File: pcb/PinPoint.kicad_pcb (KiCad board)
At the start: 2 copper layers, 35 x 32.5 mm, 2 parts, among them U1 E73-2G4M08S-52833

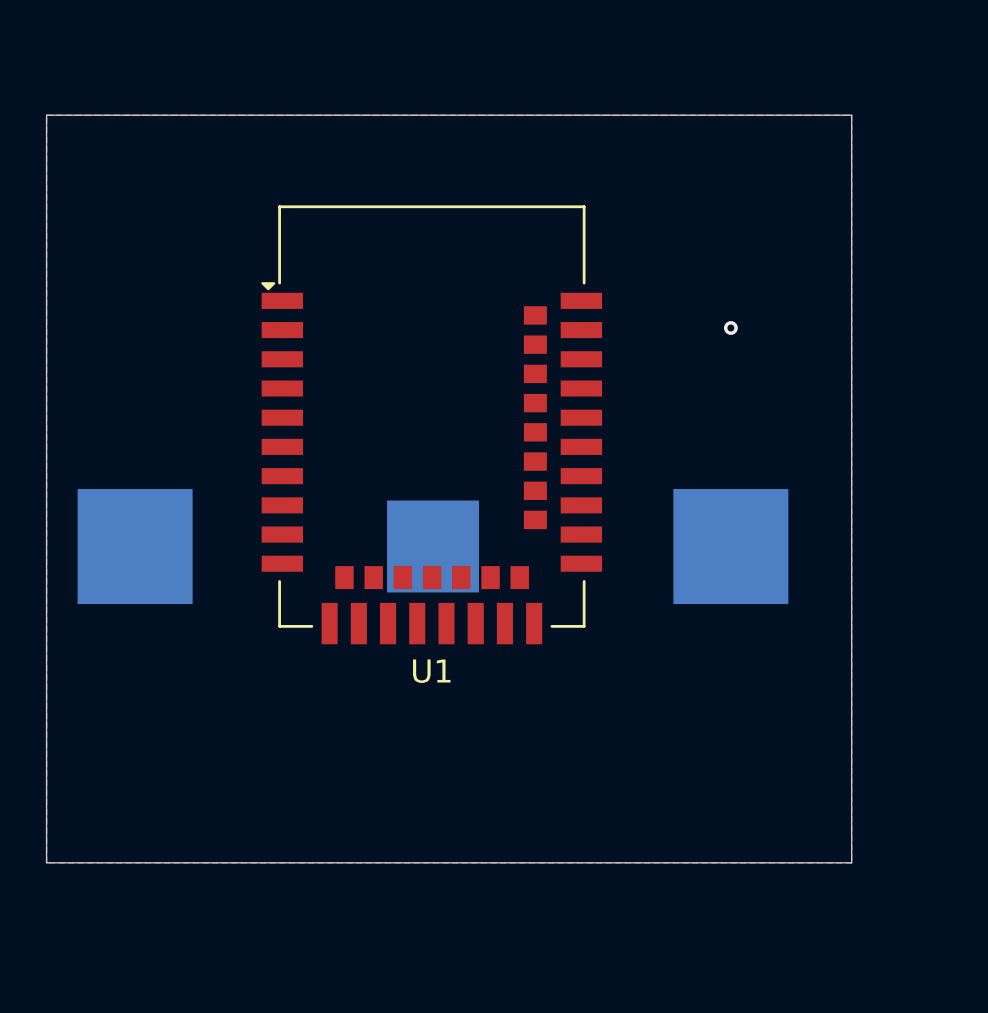
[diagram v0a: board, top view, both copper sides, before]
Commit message: Create board outline, change battery holder
Signed-off-by: Devnol <pgkoutsoumanis@gmail.com>
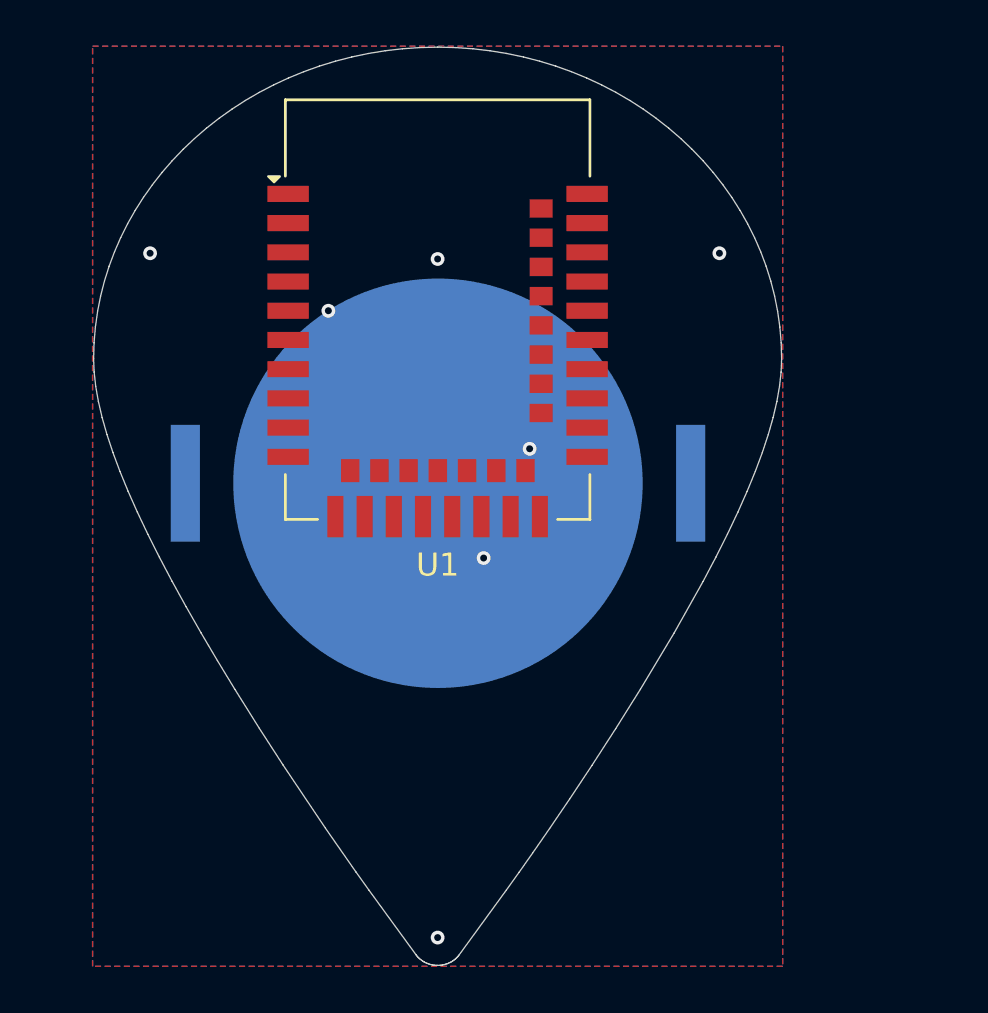
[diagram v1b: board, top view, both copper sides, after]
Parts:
- BT1: footprint Battery:BatteryHolder_Multicomp_BC-2001_1x2032 -> Battery:BatteryHolder_Keystone_3034_1x20mm
- moved U1 4.66 mm to (106.8, 41.2)
- moved BT1 2.76 mm to (106.8, 48.8)
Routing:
- net GND: vias 1 -> 7
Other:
- board size 35 x 32.5 mm -> 29.9 x 39.9 mm

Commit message: Add screw holes, debug port
Signed-off-by: Devnol <pgkoutsoumanis@gmail.com>
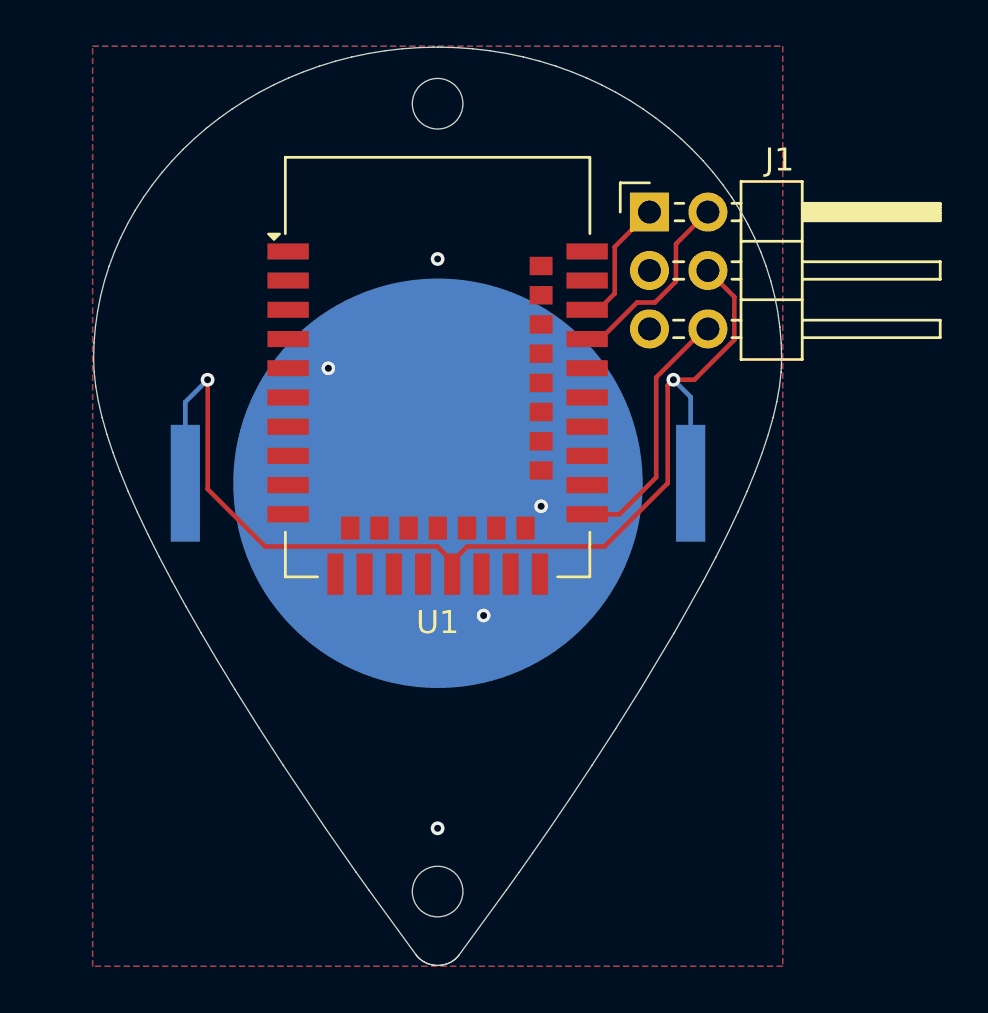
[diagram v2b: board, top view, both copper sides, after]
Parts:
- added J1: ~, Connector_PinHeader_2.54mm:PinHeader_2x03_P2.54mm_Horizontal, F.Cu at (116.0, 37.0)
- added REF**: MountingHole_2.2mm_M2_DIN965, MountingHole:MountingHole_2.2mm_M2_DIN965, F.Cu at (106.8, 32.2)
- added REF**: MountingHole_2.2mm_M2_DIN965, MountingHole:MountingHole_2.2mm_M2_DIN965, F.Cu at (106.8, 66.5)
- moved U1 2.50 mm to (106.8, 43.8)
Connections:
- net +BATT renamed VCC
- U1 pad 26: unconnected-(U1-P0.18/~{RESET}-Pad26) -> /~{RESET}
- U1 pad 37: unconnected-(U1-SWDIO-Pad37) -> /SWDIO
- U1 pad 39: unconnected-(U1-SWDCLK-Pad39) -> /SWDCLK
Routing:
- net VCC: track 0.00 -> 49.2 mm, vias 0 -> 2
- net /~{RESET}: track 0.00 -> 11.1 mm
- net /SWDIO: track 0.00 -> 8.49 mm
- net /SWDCLK: track 0.00 -> 5.66 mm
- net GND: vias 7 -> 5

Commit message: Add buzzer, include todo list for board features
Signed-off-by: Devnol <pgkoutsoumanis@gmail.com>
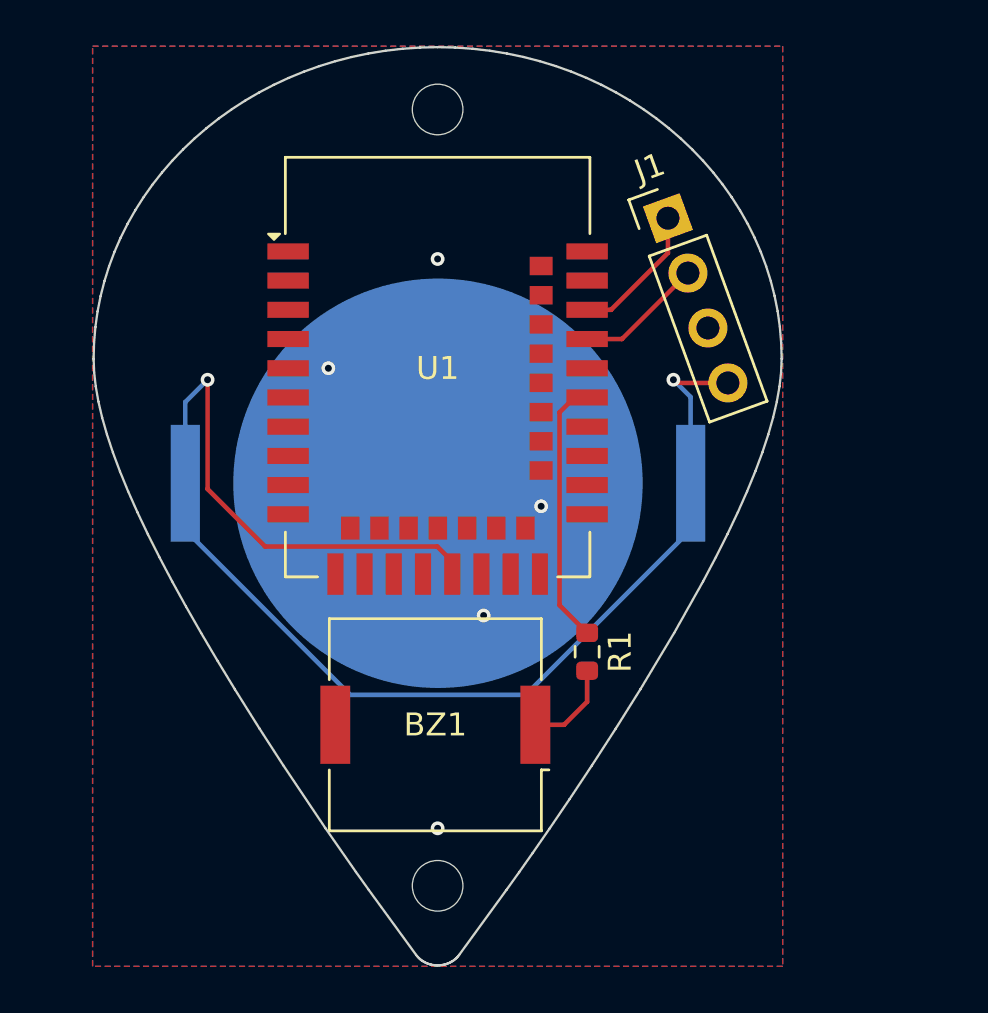
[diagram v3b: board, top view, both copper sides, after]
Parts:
- removed the REF** at (106.8, 32.2)
- removed the REF** at (106.8, 66.5)
- added BZ1: Buzzer, Buzzer_Beeper:Buzzer_Murata_PKMCS0909E, F.Cu at (106.7, 59.2)
- added R1: 100Ω, Resistor_SMD:R_0603_1608Metric, F.Cu at (113.2, 56.1)
- added REF**: MountingHole_2.2mm_M2_DIN965, MountingHole:MountingHole_2.2mm_M2_DIN965, F.Cu at (106.8, 66.2)
- added REF**: MountingHole_2.2mm_M2_DIN965, MountingHole:MountingHole_2.2mm_M2_DIN965, F.Cu at (106.8, 32.5)
- J1: footprint Connector_PinHeader_2.54mm:PinHeader_2x03_P2.54mm_Horizontal -> Connector_PinHeader_2.54mm:PinHeader_1x04_P2.54mm_Vertical
- moved J1 0.85 mm to (116.8, 37.2), turned to 20 degrees
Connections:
- U1 pad 26: /~{RESET} -> unconnected-(U1-P0.18/~{RESET}-Pad26)
- U1 pad 33: unconnected-(U1-P0.13-Pad33) -> Net-(U1-P0.13)
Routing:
- net VCC: track 49.2 -> 61.3 mm
- net Net-(U1-P0.13): track 0.00 -> 11.5 mm
- net /~{RESET}: track 11.1 -> 0.00 mm
- net Net-(BZ1-+): track 0.00 -> 4.01 mm
- net /SWDIO: track 8.49 -> 5.57 mm

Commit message: Jankily add microUSB port
Signed-off-by: Devnol <pgkoutsoumanis@gmail.com>
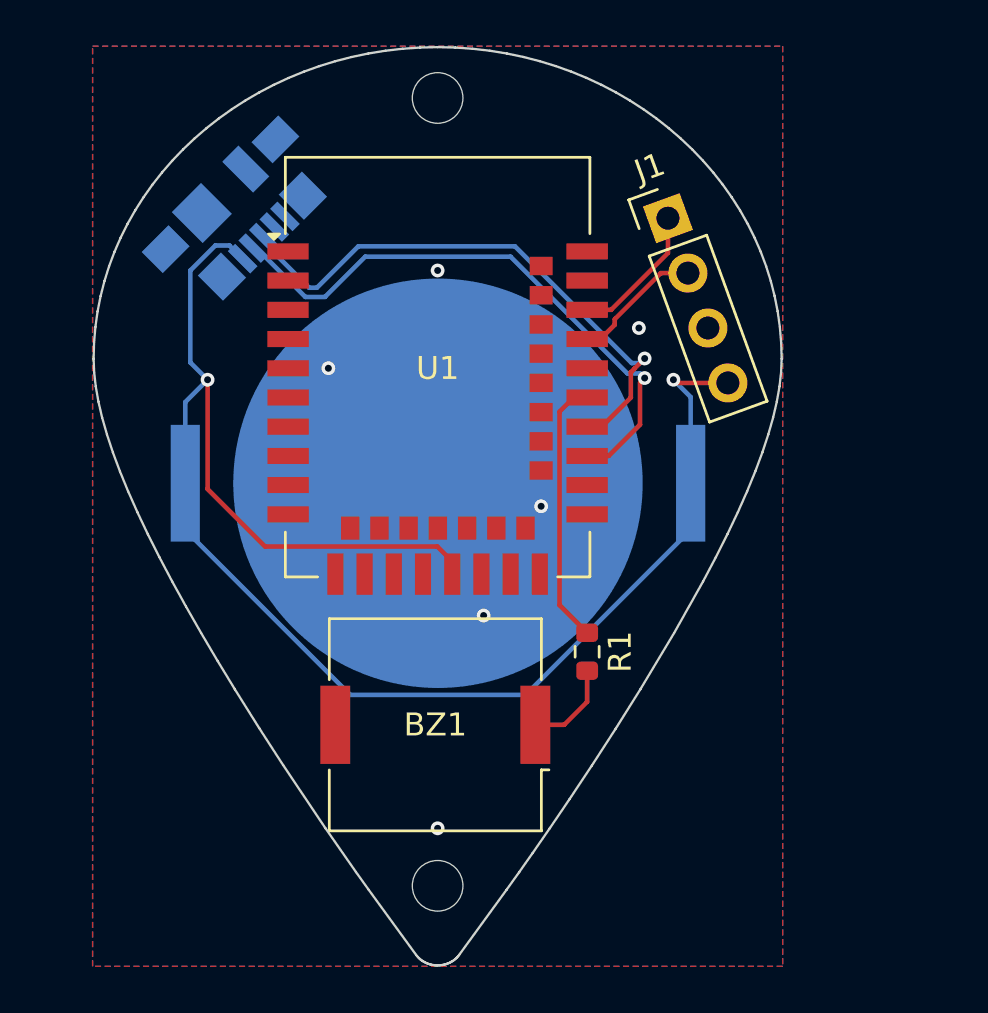
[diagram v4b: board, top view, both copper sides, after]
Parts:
- added J2: ~, Connector_USB:USB_Micro-B_Molex_47346-0001, B.Cu at (98.2, 37.0)
- moved REF** 0.50 mm to (106.8, 32.0)
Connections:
- U1 pad 29: unconnected-(U1-USB_D--Pad29) -> /USB_D-
- U1 pad 31: unconnected-(U1-USB_D+-Pad31) -> /USB_D+
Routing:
- net /USB_D-: track 0.00 -> 25.8 mm, vias 0 -> 1
- net /USB_D+: track 0.00 -> 24.9 mm, vias 0 -> 1
- net VCC: track 61.3 -> 69.4 mm
- net GND: vias 5 -> 6

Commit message: Complete board, add fab outputs
Signed-off-by: Devnol <pgkoutsoumanis@gmail.com>
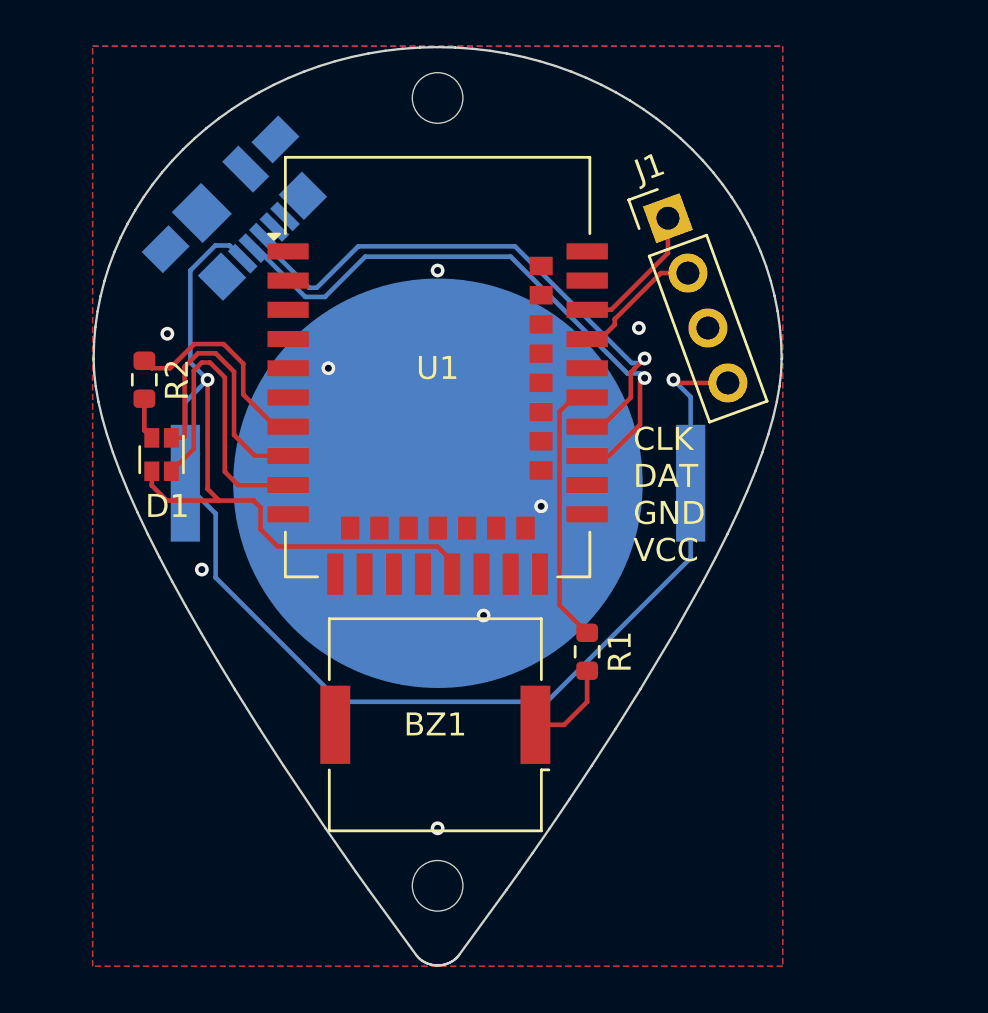
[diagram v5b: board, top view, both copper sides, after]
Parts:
- added D1: LED_RGBA, LED_SMD:LED_LiteOn_LTST-C19HE1WT, F.Cu at (94.8, 47.5)
- added R2: 25Ω, Resistor_SMD:R_0603_1608Metric, F.Cu at (94.0, 44.2)
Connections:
- U1 pad 7: unconnected-(U1-AIN0/P0.02-Pad7) -> Net-(U1-AIN0/P0.02)
- U1 pad 8: unconnected-(U1-AIN5/P0.29-Pad8) -> Net-(D1-GK)
- U1 pad 9: unconnected-(U1-AIN7/P0.31-Pad9) -> Net-(D1-BK)
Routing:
- net Net-(D1-BK): track 0.00 -> 13.6 mm
- net Net-(D1-GK): track 0.00 -> 11.8 mm
- net Net-(U1-AIN0/P0.02): track 0.00 -> 9.09 mm
- net VCC: track 69.4 -> 75.1 mm
- net Net-(D1-RK): track 0.00 -> 1.83 mm
- net GND: vias 6 -> 8
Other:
- board text added: "CLK DAT GND VCC"
- board text added: "PinPoint - rev0.1 Designed by Devnol"

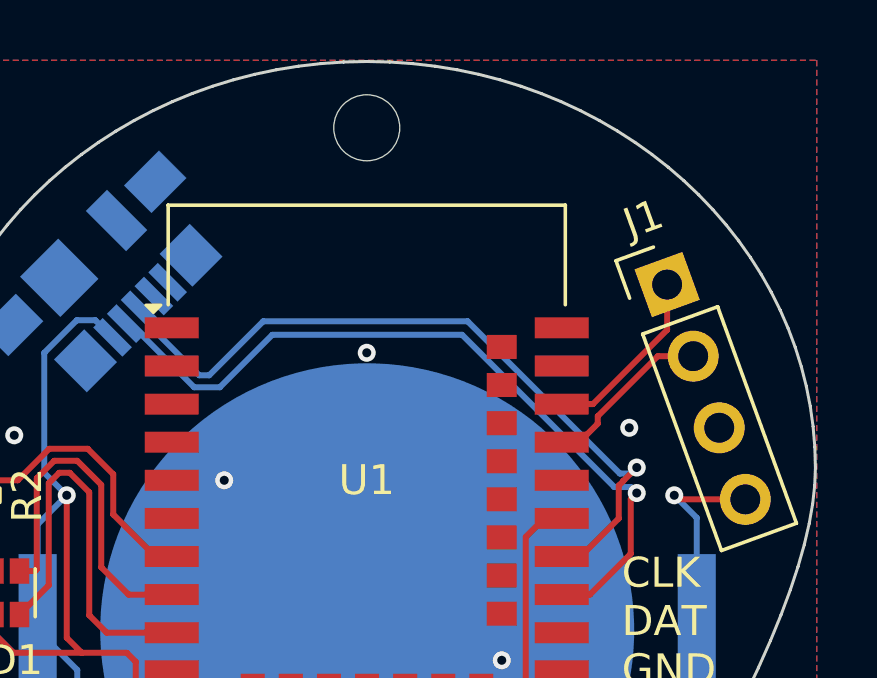
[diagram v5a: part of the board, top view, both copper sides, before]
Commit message: Add push button
Signed-off-by: Devnol <pgkoutsoumanis@gmail.com>
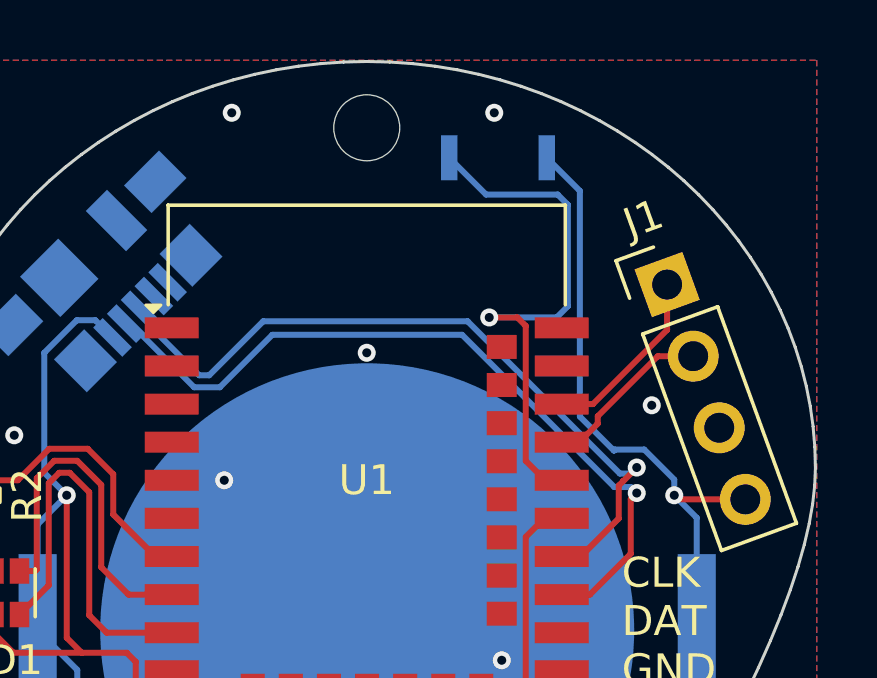
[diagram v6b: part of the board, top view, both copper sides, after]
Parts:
- added SW1: SW_Push, Button_Switch_SMD:SW_SPST_CK_KXT3, B.Cu at (111.1, 33.0)
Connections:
- U1 pad 35: unconnected-(U1-P0.24-Pad35) -> Net-(U1-P0.24)
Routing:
- net Net-(U1-P0.24): track 0.00 -> 18.1 mm, vias 0 -> 1
- net VCC: track 75.1 -> 88.8 mm
- net GND: vias 8 -> 10
